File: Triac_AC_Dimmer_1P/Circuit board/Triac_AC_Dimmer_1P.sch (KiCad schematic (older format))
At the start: 26 parts, among them J2 Conn_01x03, J3 Screw_Terminal_01x02, J4 Screw_Terminal_01x02, Q1 BTA16-600B, SW1 SW_Push, SW2 SW_Push, U1 ESP-12F, U2 4N25, U3 MOC3021M, U4 HLK-PM03

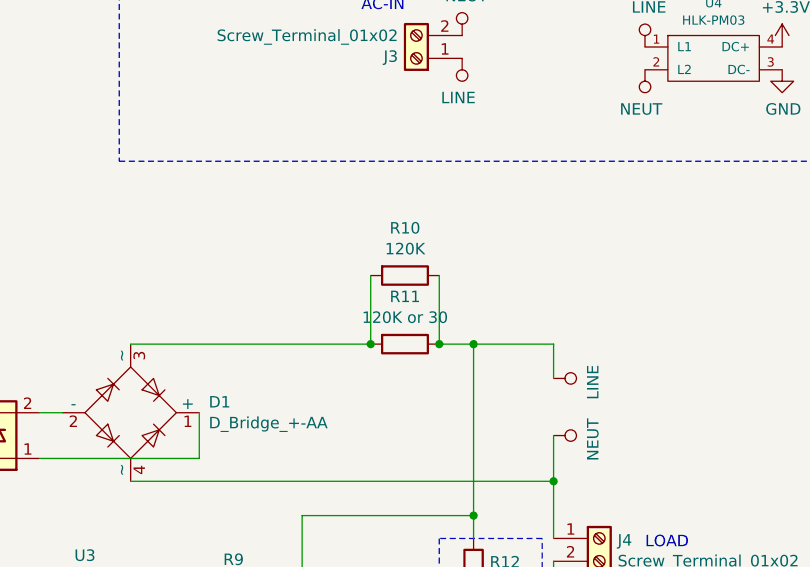
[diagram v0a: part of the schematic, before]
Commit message: Update Triac
Changed the seats for some capacitors and resistors
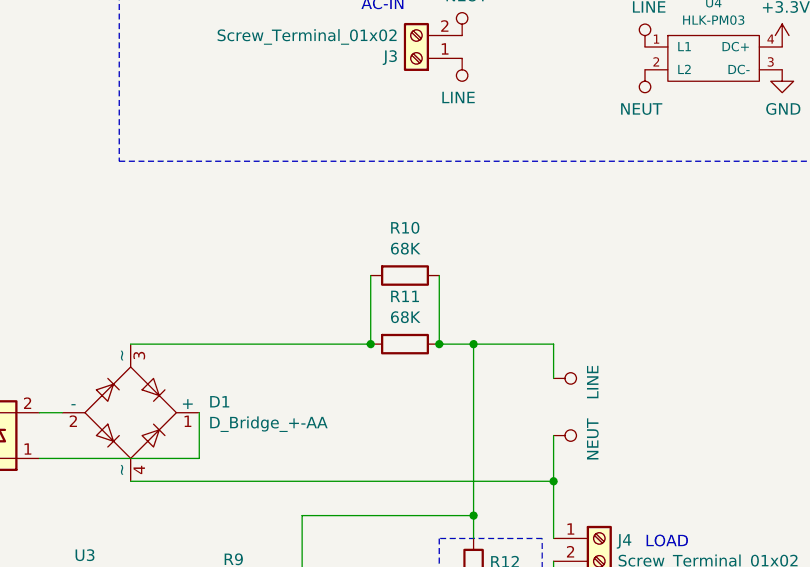
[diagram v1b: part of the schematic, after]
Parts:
- C2: footprint Capacitor_THT:C_Rect_L11.0mm_W4.3mm_P10.00mm_MKT -> Capacitor_THT:C_Rect_L13.0mm_W5.0mm_P10.00mm_FKS3_FKP3_MKS4
- D1: footprint Diode_SMD:Diode_Bridge_Vishay_DFS -> Diode_SMD:Diode_Bridge_Diotec_SO-DIL-Slim
- R10: value 120K -> 68K; footprint Resistor_THT:R_Axial_DIN0207_L6.3mm_D2.5mm_P10.16mm_Horizontal -> Resistor_THT:R_Axial_DIN0516_L15.5mm_D5.0mm_P5.08mm_Vertical
- R11: value 120K or 30 -> 68K; footprint Resistor_THT:R_Axial_DIN0207_L6.3mm_D2.5mm_P10.16mm_Horizontal -> Resistor_THT:R_Axial_DIN0516_L15.5mm_D5.0mm_P5.08mm_Vertical
- R12, R9: footprint Resistor_THT:R_Axial_DIN0207_L6.3mm_D2.5mm_P10.16mm_Horizontal -> Resistor_THT:R_Axial_DIN0516_L15.5mm_D5.0mm_P5.08mm_Vertical
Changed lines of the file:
@@
 EESchema Schematic File Version 4
+LIBS:Triac_AC_Dimmer_1P-cache
 EELAYER 26 0
 EELAYER END
@@
 F 0 "R12" H 9320 3496 50  0000 L CNN
 F 1 "39" H 9320 3405 50  0000 L CNN
-F 2 "Resistor_THT:R_Axial_DIN0207_L6.3mm_D2.5mm_P10.16mm_Horizontal" V 9180 3450 50  0001 C CNN
+F 2 "Resistor_THT:R_Axial_DIN0516_L15.5mm_D5.0mm_P5.08mm_Vertical" V 9180 3450 50  0001 C CNN
 F 3 "~" H 9250 3450 50  0001 C CNN
 	1    9250 3450
@@
 F 0 "C2" H 9365 3796 50  0000 L CNN
 F 1 "10nF" H 9365 3705 50  0000 L CNN
-F 2 "Capacitor_THT:C_Rect_L11.0mm_W4.3mm_P10.00mm_MKT" H 9288 3600 50  0001 C CNN
+F 2 "Capacitor_THT:C_Rect_L13.0mm_W5.0mm_P10.00mm_FKS3_FKP3_MKS4" H 9288 3600 50  0001 C CNN
 F 3 "~" H 9250 3750 50  0001 C CNN
 	1    9250 3750
@@
 P 8950 2450
 F 0 "R11" V 8743 2450 50  0000 C CNN
-F 1 "120K or 30" V 8834 2450 50  0000 C CNN
-F 2 "Resistor_THT:R_Axial_DIN0207_L6.3mm_D2.5mm_P10.16mm_Horizontal" V 8880 2450 50  0001 C CNN
+F 1 "68K" V 8834 2450 50  0000 C CNN
+F 2 "Resistor_THT:R_Axial_DIN0516_L15.5mm_D5.0mm_P5.08mm_Vertical" V 8880 2450 50  0001 C CNN
 F 3 "~" H 8950 2450 50  0001 C CNN
 	1    8950 2450
@@
 P 8950 2150
 F 0 "R10" V 8743 2150 50  0000 C CNN
-F 1 "120K" V 8834 2150 50  0000 C CNN
-F 2 "Resistor_THT:R_Axial_DIN0207_L6.3mm_D2.5mm_P10.16mm_Horizontal" V 8880 2150 50  0001 C CNN
+F 1 "68K" V 8834 2150 50  0000 C CNN
+F 2 "Resistor_THT:R_Axial_DIN0516_L15.5mm_D5.0mm_P5.08mm_Vertical" V 8880 2150 50  0001 C CNN
 F 3 "~" H 8950 2150 50  0001 C CNN
 	1    8950 2150
@@
 F 0 "R9" V 7993 3600 50  0000 C CNN
 F 1 "1K" V 8084 3600 50  0000 C CNN
-F 2 "Resistor_THT:R_Axial_DIN0207_L6.3mm_D2.5mm_P10.16mm_Horizontal" V 8130 3600 50  0001 C CNN
+F 2 "Resistor_THT:R_Axial_DIN0516_L15.5mm_D5.0mm_P5.08mm_Vertical" V 8130 3600 50  0001 C CNN
 F 3 "~" H 8200 3600 50  0001 C CNN
 	1    8200 3600
@@
 F 0 "D1" H 8091 2796 50  0000 L CNN
 F 1 "D_Bridge_+-AA" H 8091 2705 50  0000 L CNN
-F 2 "Diode_SMD:Diode_Bridge_Vishay_DFS" H 7750 2750 50  0001 C CNN
+F 2 "Diode_SMD:Diode_Bridge_Diotec_SO-DIL-Slim" H 7750 2750 50  0001 C CNN
 F 3 "~" H 7750 2750 50  0001 C CNN
 	1    7750 2750
